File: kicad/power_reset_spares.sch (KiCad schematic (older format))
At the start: 14 parts, among them J5 USB_B, J6 PWR, SW1 KS01Q, U16 74AHC08, U2 74AHC14, U20 MIC5504-3.3YM5, U4 74AHC32, U9 74AHC02

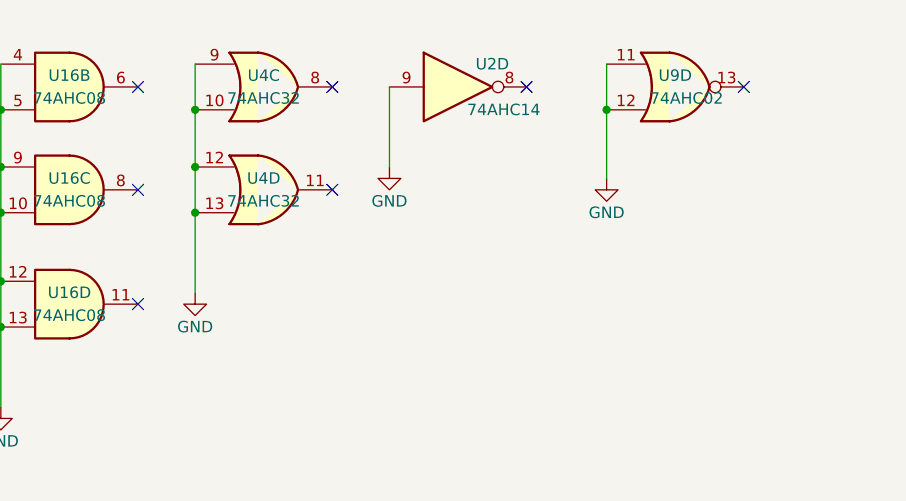
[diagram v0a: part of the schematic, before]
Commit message: SDcard interface mostly complete.
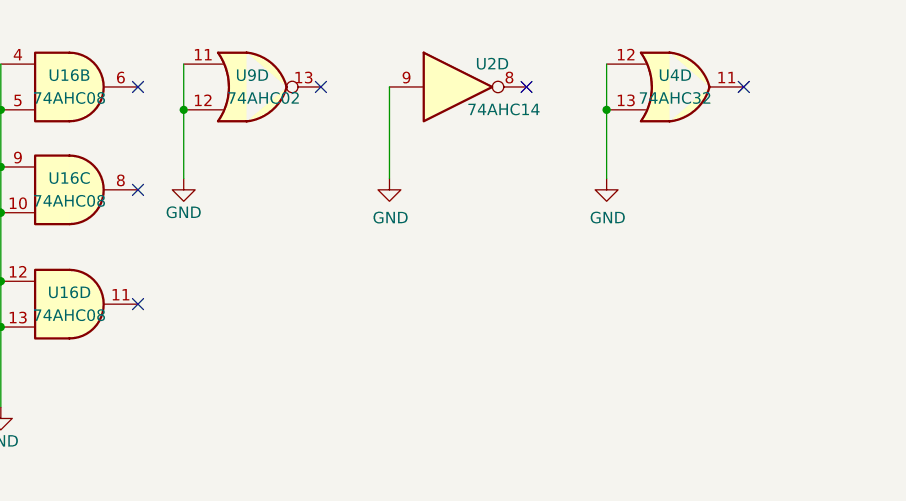
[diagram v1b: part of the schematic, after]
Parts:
- removed unit 3 of U4
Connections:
- no-connect marks 9 -> 8
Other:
- moved on the sheet: U9D
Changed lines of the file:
@@
 NoConn ~ 1400 950
-$Comp
-L 74xx:74HC14 U2
-U 4 1 59EFD892
-P 2800 950
-F 0 "U2" H 2950 1050 50  0000 C CNN
-F 1 "74AHC14" H 3000 850 50  0000 C CNN
-F 2 "Housings_DIP:DIP-14_W7.62mm_LongPads" H 2800 950 50  0001 C CNN
-F 3 "" H 2800 950 50  0001 C CNN
-	4    2800 950
-	1    0    0    -1
-$EndComp
-NoConn ~ 3100 950
-$Comp
-L power:GND #PWR073
-U 1 1 59EFDA40
-P 2500 1300
-F 0 "#PWR073" H 2500 1050 50  0001 C CNN
-F 1 "GND" H 2500 1150 50  0000 C CNN
-F 2 "" H 2500 1300 50  0001 C CNN
-F 3 "" H 2500 1300 50  0001 C CNN
-	1    2500 1300
-	1    0    0    -1
-$EndComp
 $Comp
 L 74xx:74HC02 U9
 U 4 1 59EFDB83
-P 3750 950
+P 1900 950
 AR Path="/59EFDB83" Ref="U9"  Part="4"
 AR Path="/59EFC926/59EFDB83" Ref="U9"  Part="4"
-F 0 "U9" H 3750 1000 50  0000 C CNN
-F 1 "74AHC02" H 3800 900 50  0000 C CNN
-F 2 "Housings_DIP:DIP-14_W7.62mm_LongPads" H 3750 950 50  0001 C CNN
-F 3 "" H 3750 950 50  0001 C CNN
-	4    3750 950
-	1    0    0    -1
-$EndComp
-NoConn ~ 4050 950
+F 0 "U9" H 1900 1000 50  0000 C CNN
+F 1 "74AHC02" H 1950 900 50  0000 C CNN
+F 2 "Housings_DIP:DIP-14_W7.62mm_LongPads" H 1900 950 50  0001 C CNN
+F 3 "" H 1900 950 50  0001 C CNN
+	4    1900 950
+	1    0    0    -1
+$EndComp
+NoConn ~ 2200 950
 $Comp
 L power:GND #PWR074
 U 1 1 59EFDC50
-P 3450 1350
-F 0 "#PWR074" H 3450 1100 50  0001 C CNN
-F 1 "GND" H 3450 1200 50  0000 C CNN
-F 2 "" H 3450 1350 50  0001 C CNN
-F 3 "" H 3450 1350 50  0001 C CNN
-	1    3450 1350
-	1    0    0    -1
-$EndComp
-$Comp
-L 74xx:74LS32 U4
-U 4 1 5B52E72D
-P 1950 1400
-F 0 "U4" H 1950 1450 50  0000 C CNN
-F 1 "74AHC32" H 1950 1350 50  0000 C CNN
-F 2 "Housings_DIP:DIP-14_W7.62mm_LongPads" H 1950 1400 50  0001 C CNN
-F 3 "" H 1950 1400 50  0001 C CNN
-	4    1950 1400
-	1    0    0    -1
-$EndComp
-$Comp
-L 74xx:74LS32 U4
-U 3 1 5B52E734
-P 1950 950
-F 0 "U4" H 1950 1000 50  0000 C CNN
-F 1 "74AHC32" H 1950 900 50  0000 C CNN
-F 2 "Housings_DIP:DIP-14_W7.62mm_LongPads" H 1950 950 50  0001 C CNN
-F 3 "" H 1950 950 50  0001 C CNN
-	3    1950 950
-	1    0    0    -1
-$EndComp
-NoConn ~ 2250 950
-NoConn ~ 2250 1400
-$Comp
-L power:GND #PWR075
-U 1 1 5B52E856
-P 1650 1850
-F 0 "#PWR075" H 1650 1600 50  0001 C CNN
-F 1 "GND" H 1650 1700 50  0000 C CNN
-F 2 "" H 1650 1850 50  0001 C CNN
-F 3 "" H 1650 1850 50  0001 C CNN
-	1    1650 1850
-	1    0    0    -1
-$EndComp
-Wire Wire Line
-	3450 1050 3450 1350
-Wire Wire Line
-	3450 850  3450 1050
-Connection ~ 3450 1050
-Wire Wire Line
-	2500 950  2500 1300
+P 1600 1350
+F 0 "#PWR074" H 1600 1100 50  0001 C CNN
+F 1 "GND" H 1600 1200 50  0000 C CNN
+F 2 "" H 1600 1350 50  0001 C CNN
+F 3 "" H 1600 1350 50  0001 C CNN
+	1    1600 1350
+	1    0    0    -1
+$EndComp
+Wire Wire Line
+	1600 1050 1600 1350
+Wire Wire Line
+	1600 850  1600 1050
+Connection ~ 1600 1050
 Wire Wire Line
 	800  1050 800  1300
@@
 Connection ~ 800  1800
 Connection ~ 800  2000
-Wire Wire Line
-	1650 850  1650 1050
-Wire Wire Line
-	1650 1500 1650 1850
-Wire Wire Line
-	1650 1050 1650 1300
-Connection ~ 1650 1050
-Wire Wire Line
-	1650 1300 1650 1500
-Connection ~ 1650 1300
-Connection ~ 1650 1500
 $Comp
 L Device:LED_Small_ALT D?
@@
 Text HLabel 8350 2850 2    60   Output ~ 0
 ~RESET
+$Comp
+L 74xx:74LS32 U4
+U 4 1 5CDB7434
+P 3750 950
+AR Path="/59EFC926/5CDB7434" Ref="U4"  Part="4"
+AR Path="/5CC65FE6/5CDB7434" Ref="U?"  Part="4"
+F 0 "U4" H 3750 1000 50  0000 C CNN
+F 1 "74AHC32" H 3750 900 50  0000 C CNN
+F 2 "Housings_DIP:DIP-14_W7.62mm_LongPads" H 3750 950 50  0001 C CNN
+F 3 "" H 3750 950 50  0001 C CNN
+	4    3750 950
+	1    0    0    -1
+$EndComp
+$Comp
+L 74xx:74HC14 U2
+U 4 1 5CDB743B
+P 2800 950
+AR Path="/59EFC926/5CDB743B" Ref="U2"  Part="4"
+AR Path="/5CC65FE6/5CDB743B" Ref="U?"  Part="4"
+F 0 "U2" H 2950 1050 50  0000 C CNN
+F 1 "74AHC14" H 3000 850 50  0000 C CNN
+F 2 "Housings_DIP:DIP-14_W7.62mm_LongPads" H 2800 950 50  0001 C CNN
+F 3 "" H 2800 950 50  0001 C CNN
+	4    2800 950
+	1    0    0    -1
+$EndComp
+NoConn ~ 3100 950
+NoConn ~ 4050 950
+$Comp
+L power:GND #PWR075
+U 1 1 5CDB8C4E
+P 2500 1350
+F 0 "#PWR075" H 2500 1100 50  0001 C CNN
+F 1 "GND" H 2505 1177 50  0000 C CNN
+F 2 "" H 2500 1350 50  0001 C CNN
+F 3 "" H 2500 1350 50  0001 C CNN
+	1    2500 1350
+	1    0    0    -1
+$EndComp
+$Comp
+L power:GND #PWR0101
+U 1 1 5CDB8EC9
+P 3450 1350
+F 0 "#PWR0101" H 3450 1100 50  0001 C CNN
+F 1 "GND" H 3455 1177 50  0000 C CNN
+F 2 "" H 3450 1350 50  0001 C CNN
+F 3 "" H 3450 1350 50  0001 C CNN
+	1    3450 1350
+	1    0    0    -1
+$EndComp
+Wire Wire Line
+	2500 950  2500 1350
+Wire Wire Line
+	3450 850  3450 1050
+Connection ~ 3450 1050
+Wire Wire Line
+	3450 1050 3450 1350
 $EndSCHEMATC

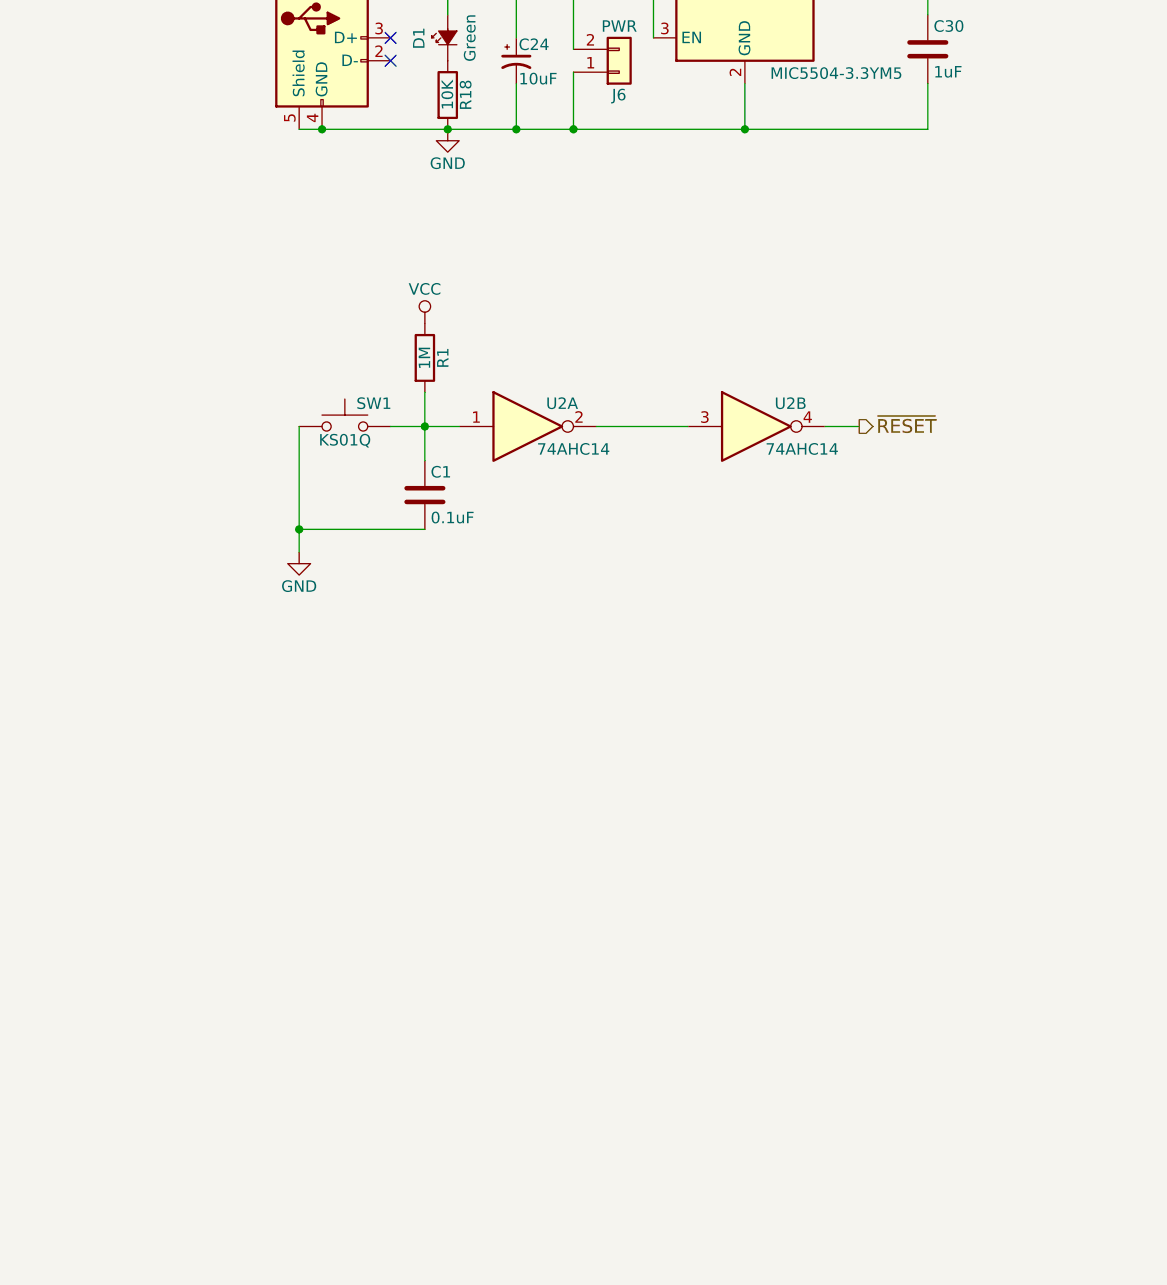
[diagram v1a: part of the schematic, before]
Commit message: Add audio output.
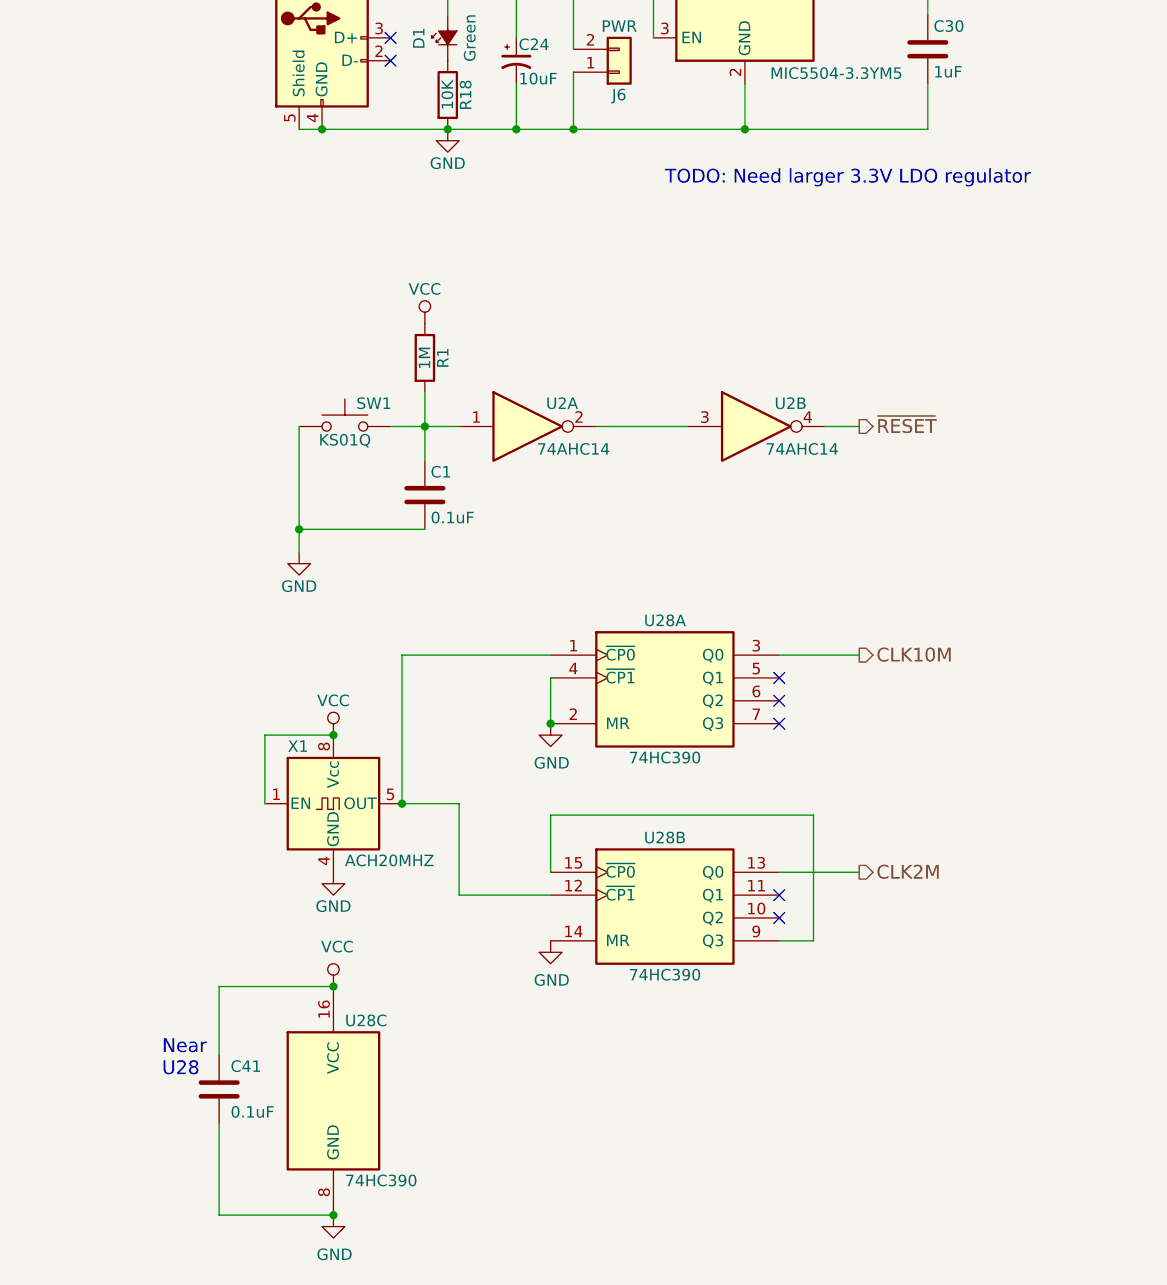
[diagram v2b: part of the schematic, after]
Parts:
- added C41: 0.1uF, symbol Device:C
- added U28: 74HC390, symbol 74xx:74LS390
- added X1: ACH20MHZ, Oscillators:Oscillator_DIP-8, symbol Oscillator:CXO_DIP8
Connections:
- net GND: now also C41.2, U28.14 (MR), U28.2 (MR), U28.4 (~CP1), U28.8 (GND), X1.4 (GND)
- net VCC: now also C41.1, U28.16 (VCC), X1.1 (EN), X1.8 (Vcc)
- new net: U28.1 (~CP0), U28.12 (~CP1), X1.5 (OUT)
- new net: U28.15 (~CP0), U28.9 (Q3)
- new net CLK10M: U28.3 (Q0)
- new net CLK2M: U28.13 (Q0)
- no-connect marks 8 -> 13
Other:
- note added: "Near\nU28"
- note added: "TODO: Need larger 3.3V LDO regulator"
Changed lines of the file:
@@
 EESchema Schematic File Version 4
 LIBS:z80-cache
-EELAYER 26 0
+EELAYER 29 0
 EELAYER END
 $Descr USLetter 11000 8500
 encoding utf-8
-Sheet 7 10
+Sheet 7 11
 Title "Power, reset, and spares"
 Date "2018-07-20"
@@
 Wire Wire Line
 	3450 1050 3450 1350
+Text Notes 7500 1800 0    60   ~ 0
+TODO: Need larger 3.3V LDO regulator
+$Comp
+L Oscillator:CXO_DIP8 X?
+U 1 1 5CA34C8B
+P 6050 4500
+AR Path="/5CA34C8B" Ref="X?"  Part="1"
+AR Path="/59EFC926/5CA34C8B" Ref="X1"  Part="1"
+F 0 "X1" H 5850 4750 50  0000 L CNN
+F 1 "ACH20MHZ" H 6100 4250 50  0000 L CNN
+F 2 "Oscillators:Oscillator_DIP-8" H 6500 4150 50  0001 C CNN
+F 3 "http://www.abracon.com/Oscillators/ACH.pdf" H 5950 4500 50  0001 C CNN
+	1    6050 4500
+	1    0    0    -1
+$EndComp
+$Comp
+L power:GND #PWR?
+U 1 1 5CA34C91
+P 6050 4800
+AR Path="/5CA34C91" Ref="#PWR?"  Part="1"
+AR Path="/59EFC926/5CA34C91" Ref="#PWR06"  Part="1"
+F 0 "#PWR06" H 6050 4550 50  0001 C CNN
+F 1 "GND" H 6050 4650 50  0000 C CNN
+F 2 "" H 6050 4800 50  0001 C CNN
+F 3 "" H 6050 4800 50  0001 C CNN
+	1    6050 4800
+	1    0    0    -1
+$EndComp
+$Comp
+L power:VCC #PWR?
+U 1 1 5CA34C97
+P 6050 4200
+AR Path="/5CA34C97" Ref="#PWR?"  Part="1"
+AR Path="/59EFC926/5CA34C97" Ref="#PWR03"  Part="1"
+F 0 "#PWR03" H 6050 4050 50  0001 C CNN
+F 1 "VCC" H 6050 4350 50  0000 C CNN
+F 2 "" H 6050 4200 50  0001 C CNN
+F 3 "" H 6050 4200 50  0001 C CNN
+	1    6050 4200
+	1    0    0    -1
+$EndComp
+Wire Wire Line
+	6050 4200 5750 4200
+Wire Wire Line
+	5750 4200 5750 4500
+Connection ~ 6050 4200
+$Comp
+L 74xx:74LS390 U28
+U 1 1 5CA35A3F
+P 7500 3950
+F 0 "U28" H 7500 4200 50  0000 C CNN
+F 1 "74HC390" H 7500 3600 50  0000 C CNN
+F 2 "" H 7500 3950 50  0001 C CNN
+F 3 "http://www.ti.com/lit/gpn/sn74LS390" H 7500 3950 50  0001 C CNN
+	1    7500 3950
+	1    0    0    -1
+$EndComp
+$Comp
+L 74xx:74LS390 U28
+U 2 1 5CA3A042
+P 7500 4900
+F 0 "U28" H 7500 5150 50  0000 C CNN
+F 1 "74HC390" H 7500 4550 50  0000 C CNN
+F 2 "" H 7500 4900 50  0001 C CNN
+F 3 "http://www.ti.com/lit/gpn/sn74LS390" H 7500 4900 50  0001 C CNN
+	2    7500 4900
+	1    0    0    -1
+$EndComp
+$Comp
+L 74xx:74LS390 U28
+U 3 1 5CA3A8D7
+P 6050 5800
+F 0 "U28" H 6100 6150 50  0000 L CNN
+F 1 "74HC390" H 6100 5450 50  0000 L CNN
+F 2 "" H 6050 5800 50  0001 C CNN
+F 3 "http://www.ti.com/lit/gpn/sn74LS390" H 6050 5800 50  0001 C CNN
+	3    6050 5800
+	1    0    0    -1
+$EndComp
+$Comp
+L power:VCC #PWR0126
+U 1 1 5CA3F4B4
+P 6050 5300
+F 0 "#PWR0126" H 6050 5150 50  0001 C CNN
+F 1 "VCC" H 6067 5473 50  0000 C CNN
+F 2 "" H 6050 5300 50  0001 C CNN
+F 3 "" H 6050 5300 50  0001 C CNN
+	1    6050 5300
+	1    0    0    -1
+$EndComp
+$Comp
+L power:GND #PWR0127
+U 1 1 5CA3FB27
+P 6050 6300
+F 0 "#PWR0127" H 6050 6050 50  0001 C CNN
+F 1 "GND" H 6055 6127 50  0000 C CNN
+F 2 "" H 6050 6300 50  0001 C CNN
+F 3 "" H 6050 6300 50  0001 C CNN
+	1    6050 6300
+	1    0    0    -1
+$EndComp
+$Comp
+L power:GND #PWR0128
+U 1 1 5CA407E1
+P 7000 4150
+F 0 "#PWR0128" H 7000 3900 50  0001 C CNN
+F 1 "GND" H 7005 3977 50  0000 C CNN
+F 2 "" H 7000 4150 50  0001 C CNN
+F 3 "" H 7000 4150 50  0001 C CNN
+	1    7000 4150
+	1    0    0    -1
+$EndComp
+$Comp
+L power:GND #PWR0129
+U 1 1 5CA40E15
+P 7000 5100
+F 0 "#PWR0129" H 7000 4850 50  0001 C CNN
+F 1 "GND" H 7005 4927 50  0000 C CNN
+F 2 "" H 7000 5100 50  0001 C CNN
+F 3 "" H 7000 5100 50  0001 C CNN
+	1    7000 5100
+	1    0    0    -1
+$EndComp
+Wire Wire Line
+	6350 4500 6350 3850
+Wire Wire Line
+	6350 3850 7000 3850
+Text HLabel 8350 3850 2    60   Output ~ 0
+CLK10M
+Wire Wire Line
+	8000 3850 8350 3850
+NoConn ~ 8000 3950
+NoConn ~ 8000 4050
+NoConn ~ 8000 4150
+Wire Wire Line
+	7000 3950 7000 4150
+Connection ~ 7000 4150
+Wire Wire Line
+	7000 4900 6600 4900
+Wire Wire Line
+	6600 4900 6600 4500
+Wire Wire Line
+	6600 4500 6350 4500
+Connection ~ 6350 4500
+Wire Wire Line
+	8000 5100 8150 5100
+Wire Wire Line
+	8150 5100 8150 4550
+Wire Wire Line
+	8150 4550 7000 4550
+Wire Wire Line
+	7000 4550 7000 4800
+NoConn ~ 8000 4900
+NoConn ~ 8000 5000
+Text HLabel 8350 4800 2    60   Output ~ 0
+CLK2M
+Wire Wire Line
+	8000 4800 8350 4800
+$Comp
+L Device:C C41
+U 1 1 5CA593DD
+P 5550 5750
+F 0 "C41" H 5600 5850 50  0000 L CNN
+F 1 "0.1uF" H 5600 5650 50  0000 L CNN
+F 2 "" H 5588 5600 50  0001 C CNN
+F 3 "~" H 5550 5750 50  0001 C CNN
+	1    5550 5750
+	1    0    0    -1
+$EndComp
+Wire Wire Line
+	6050 5300 5550 5300
+Wire Wire Line
+	5550 5300 5550 5600
+Wire Wire Line
+	5550 5900 5550 6300
+Wire Wire Line
+	5550 6300 6050 6300
+Connection ~ 6050 5300
+Connection ~ 6050 6300
+Text Notes 5300 5700 0    60   ~ 0
+Near\nU28
 $EndSCHEMATC

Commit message: First complete version of ZED-80 schematic.
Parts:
- removed U20: MIC5504-3.3YM5, TO_SOT_Packages_SMD:SOT-23-5, symbol Regulator_Linear:MIC5504-3.3YM5
- added C45: 4.7uF, symbol Device:C
- added U20: AP2114HA-33, symbol Regulator_Linear:AP7361C-33E
- C30: value 1uF -> 4.7uF
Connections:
- net +3V3: now also U20.3 (VO)
- net GND: now also C45.2, U20.2 (GND)
- net VCC: now also C45.1, U20.1 (VI)
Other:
- note removed: "TODO: Need larger 3.3V LDO regulator"
- moved on the sheet: C30
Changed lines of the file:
@@
 EESchema Schematic File Version 4
-LIBS:z80-cache
 EELAYER 29 0
 EELAYER END
@@
 Sheet 7 11
 Title "Power, reset, and spares"
-Date "2018-07-20"
-Rev "12"
+Date "2019-04-03"
+Rev "1"
 Comp ""
 Comment1 ""
@@
 $EndComp
 $Comp
-L Regulator_Linear:MIC5504-3.3YM5 U?
-U 1 1 5CB1CFC4
-P 7850 1050
-AR Path="/5CB1CFC4" Ref="U?"  Part="1"
-AR Path="/59EFC926/5CB1CFC4" Ref="U20"  Part="1"
-F 0 "U20" H 7600 1300 50  0000 C CNN
-F 1 "MIC5504-3.3YM5" H 8250 794 50  0000 C CNN
-F 2 "TO_SOT_Packages_SMD:SOT-23-5" H 7850 650 50  0001 C CNN
-F 3 "" H 7850 1250 50  0001 C CNN
-	1    7850 1050
-	1    0    0    -1
-$EndComp
-$Comp
 L power:+3V3 #PWR?
 U 1 1 5CB1CFCB
-P 8450 950
+P 8750 950
 AR Path="/5CB1CFCB" Ref="#PWR?"  Part="1"
 AR Path="/59EFC926/5CB1CFCB" Ref="#PWR096"  Part="1"
-F 0 "#PWR096" H 8450 800 50  0001 C CNN
-F 1 "+3V3" H 8450 1090 50  0000 C CNN
-F 2 "" H 8450 950 50  0001 C CNN
-F 3 "" H 8450 950 50  0001 C CNN
-	1    8450 950
+F 0 "#PWR096" H 8750 800 50  0001 C CNN
+F 1 "+3V3" H 8750 1090 50  0000 C CNN
+F 2 "" H 8750 950 50  0001 C CNN
+F 3 "" H 8750 950 50  0001 C CNN
+	1    8750 950
 	1    0    0    -1
 $EndComp
@@
 L Device:C C?
 U 1 1 5CB1CFD1
-P 8650 1200
+P 8950 1200
 AR Path="/5CB1CFD1" Ref="C?"  Part="1"
 AR Path="/59EFC926/5CB1CFD1" Ref="C30"  Part="1"
-F 0 "C30" H 8675 1300 50  0000 L CNN
-F 1 "1uF" H 8675 1100 50  0000 L CNN
-F 2 "" H 8688 1050 50  0001 C CNN
-F 3 "" H 8650 1200 50  0001 C CNN
-	1    8650 1200
+F 0 "C30" H 8975 1300 50  0000 L CNN
+F 1 "4.7uF" H 8975 1100 50  0000 L CNN
+F 2 "" H 8988 1050 50  0001 C CNN
+F 3 "" H 8950 1200 50  0001 C CNN
+	1    8950 1200
 	1    0    0    -1
 $EndComp
@@
 Wire Wire Line
 	7100 1550 7100 1300
-Wire Wire Line
-	7850 1550 7850 1350
 Connection ~ 7100 950
 Wire Wire Line
-	8650 950  8650 1050
-Wire Wire Line
-	8250 950  8450 950
-Connection ~ 8450 950
-Wire Wire Line
-	8650 1550 8650 1350
-Connection ~ 7850 1550
+	8950 950  8950 1050
+Connection ~ 8750 950
+Wire Wire Line
+	8950 1550 8950 1350
+Connection ~ 8150 1550
 Wire Wire Line
 	6000 1550 6550 1550
@@
 	6850 1550 7100 1550
 Wire Wire Line
-	8450 950  8650 950
-Wire Wire Line
-	7850 1550 8650 1550
-Wire Wire Line
-	7100 950  7450 950
-Wire Wire Line
-	7450 1150 7450 950
-Connection ~ 7450 950
-Wire Wire Line
-	7100 1550 7850 1550
-Connection ~ 7100 1550
+	8750 950  8950 950
+Wire Wire Line
+	8150 1550 8950 1550
 $Comp
 L Switch:SW_Push SW?
@@
 Wire Wire Line
 	3450 1050 3450 1350
-Text Notes 7500 1800 0    60   ~ 0
-TODO: Need larger 3.3V LDO regulator
 $Comp
 L Oscillator:CXO_DIP8 X?
@@
 Text Notes 5300 5700 0    60   ~ 0
 Near\nU28
+$Comp
+L Regulator_Linear:AP7361C-33E U20
+U 1 1 5CDAFB55
+P 8150 950
+F 0 "U20" H 8000 1100 50  0000 C CNN
+F 1 "AP2114HA-33" H 8450 700 50  0000 C CNN
+F 2 "" H 8150 1175 50  0001 C CIN
+F 3 "" H 8150 900 50  0001 C CNN
+	1    8150 950
+	1    0    0    -1
+$EndComp
+Wire Wire Line
+	8150 1250 8150 1550
+Wire Wire Line
+	8450 950  8750 950
+$Comp
+L Device:C C?
+U 1 1 5CDBB06C
+P 7650 1200
+AR Path="/5CDBB06C" Ref="C?"  Part="1"
+AR Path="/59EFC926/5CDBB06C" Ref="C45"  Part="1"
+F 0 "C45" H 7675 1300 50  0000 L CNN
+F 1 "4.7uF" H 7675 1100 50  0000 L CNN
+F 2 "" H 7688 1050 50  0001 C CNN
+F 3 "" H 7650 1200 50  0001 C CNN
+	1    7650 1200
+	1    0    0    -1
+$EndComp
+Wire Wire Line
+	7100 950  7650 950
+Wire Wire Line
+	7100 1550 7650 1550
+Connection ~ 7100 1550
+Wire Wire Line
+	7650 1350 7650 1550
+Connection ~ 7650 1550
+Wire Wire Line
+	7650 1550 8150 1550
+Wire Wire Line
+	7650 1050 7650 950
+Connection ~ 7650 950
+Wire Wire Line
+	7650 950  7850 950
 $EndSCHEMATC
